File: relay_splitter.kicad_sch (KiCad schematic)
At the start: 7 parts, among them J10 Pads for coax, K6 RY-12W-K, Q6 MMBT3904

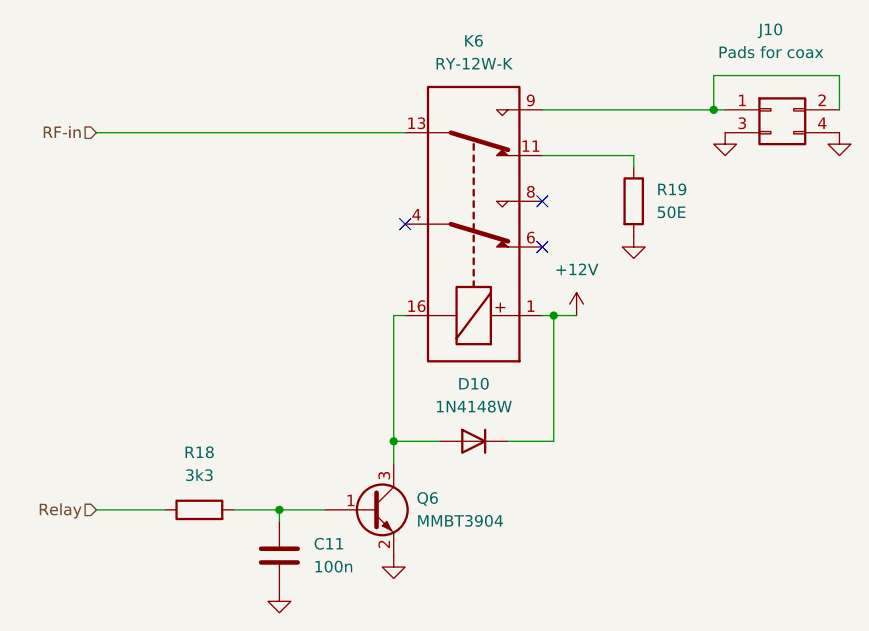
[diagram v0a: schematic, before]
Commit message: changed to 1 to 6
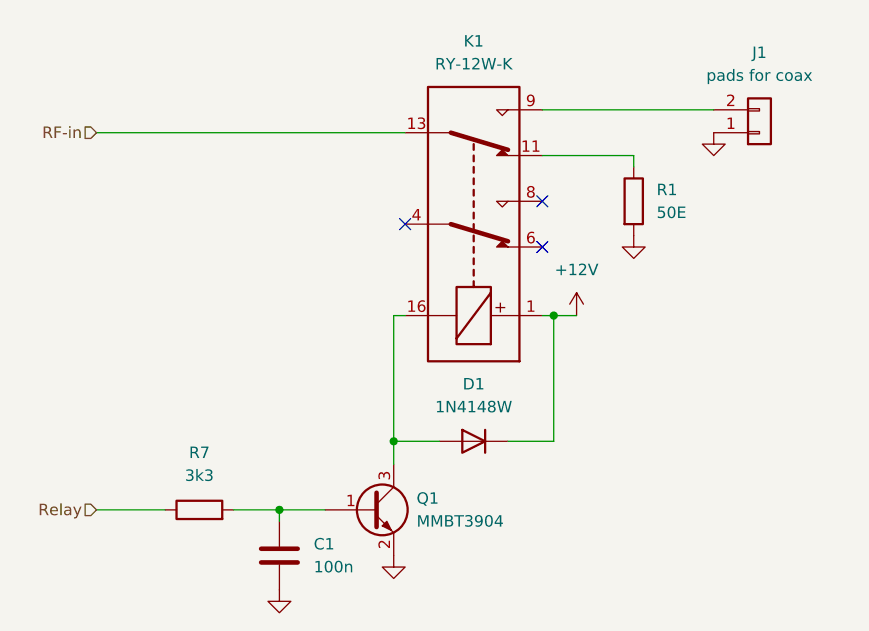
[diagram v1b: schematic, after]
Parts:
- removed J10: Pads for coax, Connector_PinHeader_2.54mm:PinHeader_2x02_P2.54mm_Vertical, symbol Components:Conn_02x02_Odd_Even
- added J1: pads for coax, Components:Coax_pad, symbol Components:Conn_01x02
- renumbered C11 to C1, D10 to D1, K6 to K1, Q6 to Q1, R19 to R1, R18 to R7
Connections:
- net GND: now also J1.1 (Pin_1)
- net at K1.9: now also J1.2 (Pin_2)
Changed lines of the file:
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@@
   (junction (at 127 107.95) (diameter 0) (color 0 0 0 0)
-  )
-  (junction (at 162.56 71.12) (diameter 0) (color 0 0 0 0)
   )
   (no_connect (at 128.27 83.82))
@@
     (stroke (width 0) (type default) (color 0 0 0 0))
   )
-  (wire (pts (xy 176.53 71.12) (xy 176.53 67.31))
-    (stroke (width 0) (type default) (color 0 0 0 0))
-  )
   (wire (pts (xy 127 110.49) (xy 127 107.95))
     (stroke (width 0) (type default) (color 0 0 0 0))
@@
     (stroke (width 0) (type default) (color 0 0 0 0))
   )
-  (wire (pts (xy 176.53 67.31) (xy 162.56 67.31))
-    (stroke (width 0) (type default) (color 0 0 0 0))
-  )
   (wire (pts (xy 153.67 76.2) (xy 153.67 77.47))
     (stroke (width 0) (type default) (color 0 0 0 0))
@@
     (stroke (width 0) (type default) (color 0 0 0 0))
   )
-  (wire (pts (xy 162.56 67.31) (xy 162.56 71.12))
-    (stroke (width 0) (type default) (color 0 0 0 0))
-  )
   (wire (pts (xy 93.98 73.66) (xy 128.27 73.66))
     (stroke (width 0) (type default) (color 0 0 0 0))
@@
   )
   (wire (pts (xy 143.51 71.12) (xy 162.56 71.12))
-    (stroke (width 0) (type default) (color 0 0 0 0))
-  )
-  (wire (pts (xy 162.56 71.12) (xy 163.83 71.12))
     (stroke (width 0) (type default) (color 0 0 0 0))
   )
@@
     (effects (font (size 1.27 1.27)) (justify right))
   )
-  (symbol (lib_id "power:GND") (at 176.53 73.66 0) (unit 1)
-    (in_bom yes) (on_board yes) (fields_autoplaced)
-    (property "Reference" "#PWR055" (id 0) (at 176.53 80.01 0)
-      (effects (font (size 1.27 1.27)) hide)
-    )
-    (property "Value" "GND" (id 1) (at 176.53 78.74 0)
-      (effects (font (size 1.27 1.27)) hide)
-    )
-    (property "Footprint" "" (id 2) (at 176.53 73.66 0)
-      (effects (font (size 1.27 1.27)) hide)
-    )
-    (property "Datasheet" "" (id 3) (at 176.53 73.66 0)
-      (effects (font (size 1.27 1.27)) hide)
-    )
-    (pin "1")
-  )
   (symbol (lib_id "power:+12V") (at 147.32 93.98 0) (unit 1)
     (in_bom yes) (on_board yes) (fields_autoplaced)
-    (property "Reference" "#PWR052" (id 0) (at 147.32 97.79 0)
+    (property "Reference" "#PWR045" (id 0) (at 147.32 97.79 0)
       (effects (font (size 1.27 1.27)) hide)
     )
@@
   (symbol (lib_id "Device:R") (at 105.41 115.57 90) (unit 1)
     (in_bom yes) (on_board yes) (fields_autoplaced)
-    (property "Reference" "R18" (id 0) (at 105.41 109.22 90))
+    (property "Reference" "R7" (id 0) (at 105.41 109.22 90))
     (property "Value" "3k3" (id 1) (at 105.41 111.76 90))
     (property "Footprint" "Resistor_SMD:R_0603_1608Metric_Pad0.98x0.95mm_HandSolder" (id 2) (at 105.41 117.348 90)
@@
   (symbol (lib_id "Transistor_BJT:MMBT3904") (at 124.46 115.57 0) (unit 1)
     (in_bom yes) (on_board yes) (fields_autoplaced)
-    (property "Reference" "Q6" (id 0) (at 129.54 114.2999 0)
+    (property "Reference" "Q1" (id 0) (at 129.54 114.2999 0)
       (effects (font (size 1.27 1.27)) (justify left))
     )
@@
     (pin "3")
   )
+  (symbol (lib_id "Components:Conn_01x02") (at 167.64 73.66 0) (mirror x) (unit 1)
+    (in_bom yes) (on_board yes) (fields_autoplaced)
+    (property "Reference" "J1" (id 0) (at 167.64 64.77 0))
+    (property "Value" "pads for coax" (id 1) (at 167.64 67.31 0))
+    (property "Footprint" "Components:Coax_pad" (id 2) (at 167.64 73.66 0)
+      (effects (font (size 1.27 1.27)) hide)
+    )
+    (property "Datasheet" "~" (id 3) (at 167.64 73.66 0)
+      (effects (font (size 1.27 1.27)) hide)
+    )
+    (pin "1")
+    (pin "2")
+  )
   (symbol (lib_id "Device:C") (at 114.3 120.65 0) (unit 1)
     (in_bom yes) (on_board yes) (fields_autoplaced)
-    (property "Reference" "C11" (id 0) (at 118.11 119.3799 0)
+    (property "Reference" "C1" (id 0) (at 118.11 119.3799 0)
       (effects (font (size 1.27 1.27)) (justify left))
     )
@@
     (pin "2")
   )
-  (symbol (lib_id "Components:Conn_02x02_Odd_Even") (at 168.91 71.12 0) (unit 1)
-    (in_bom yes) (on_board yes)
-    (property "Reference" "J10" (id 0) (at 168.91 62.23 0))
-    (property "Value" "Pads for coax" (id 1) (at 168.91 64.77 0))
-    (property "Footprint" "Connector_PinHeader_2.54mm:PinHeader_2x02_P2.54mm_Vertical" (id 2) (at 168.91 71.12 0)
-      (effects (font (size 1.27 1.27)) hide)
-    )
-    (property "Datasheet" "~" (id 3) (at 168.91 71.12 0)
-      (effects (font (size 1.27 1.27)) hide)
-    )
-    (pin "1")
-    (pin "2")
-    (pin "3")
-    (pin "4")
-  )
-  (symbol (lib_id "power:GND") (at 163.83 73.66 0) (unit 1)
-    (in_bom yes) (on_board yes) (fields_autoplaced)
-    (property "Reference" "#PWR054" (id 0) (at 163.83 80.01 0)
-      (effects (font (size 1.27 1.27)) hide)
-    )
-    (property "Value" "GND" (id 1) (at 163.83 78.74 0)
-      (effects (font (size 1.27 1.27)) hide)
-    )
-    (property "Footprint" "" (id 2) (at 163.83 73.66 0)
-      (effects (font (size 1.27 1.27)) hide)
-    )
-    (property "Datasheet" "" (id 3) (at 163.83 73.66 0)
-      (effects (font (size 1.27 1.27)) hide)
-    )
-    (pin "1")
-  )
   (symbol (lib_id "Components:RY-12W-K") (at 135.89 83.82 270) (mirror x) (unit 1)
     (in_bom yes) (on_board yes) (fields_autoplaced)
-    (property "Reference" "K6" (id 0) (at 135.89 63.5 90))
+    (property "Reference" "K1" (id 0) (at 135.89 63.5 90))
     (property "Value" "RY-12W-K" (id 1) (at 135.89 66.04 90))
     (property "Footprint" "Components:RELAY_RY-12W-K" (id 2) (at 137.16 69.85 0)
@@
   (symbol (lib_id "power:GND") (at 127 120.65 0) (unit 1)
     (in_bom yes) (on_board yes) (fields_autoplaced)
-    (property "Reference" "#PWR051" (id 0) (at 127 127 0)
+    (property "Reference" "#PWR044" (id 0) (at 127 127 0)
       (effects (font (size 1.27 1.27)) hide)
     )
@@
   (symbol (lib_id "Device:R") (at 153.67 81.28 0) (unit 1)
     (in_bom yes) (on_board yes) (fields_autoplaced)
-    (property "Reference" "R19" (id 0) (at 156.21 80.0099 0)
+    (property "Reference" "R1" (id 0) (at 156.21 80.0099 0)
       (effects (font (size 1.27 1.27)) (justify left))
     )
@@
   (symbol (lib_id "power:GND") (at 153.67 85.09 0) (unit 1)
     (in_bom yes) (on_board yes) (fields_autoplaced)
-    (property "Reference" "#PWR053" (id 0) (at 153.67 91.44 0)
+    (property "Reference" "#PWR046" (id 0) (at 153.67 91.44 0)
       (effects (font (size 1.27 1.27)) hide)
     )
@@
     (pin "1")
   )
+  (symbol (lib_id "power:GND") (at 162.56 73.66 0) (unit 1)
+    (in_bom yes) (on_board yes) (fields_autoplaced)
+    (property "Reference" "#PWR07" (id 0) (at 162.56 80.01 0)
+      (effects (font (size 1.27 1.27)) hide)
+    )
+    (property "Value" "GND" (id 1) (at 162.56 78.74 0)
+      (effects (font (size 1.27 1.27)) hide)
+    )
+    (property "Footprint" "" (id 2) (at 162.56 73.66 0)
+      (effects (font (size 1.27 1.27)) hide)
+    )
+    (property "Datasheet" "" (id 3) (at 162.56 73.66 0)
+      (effects (font (size 1.27 1.27)) hide)
+    )
+    (pin "1")
+  )
   (symbol (lib_id "power:GND") (at 114.3 124.46 0) (unit 1)
     (in_bom yes) (on_board yes) (fields_autoplaced)
-    (property "Reference" "#PWR050" (id 0) (at 114.3 130.81 0)
+    (property "Reference" "#PWR043" (id 0) (at 114.3 130.81 0)
       (effects (font (size 1.27 1.27)) hide)
     )
@@
   (symbol (lib_id "Diode:1N4148W") (at 135.89 107.95 0) (mirror y) (unit 1)
     (in_bom yes) (on_board yes) (fields_autoplaced)
-    (property "Reference" "D10" (id 0) (at 135.89 101.6 0))
+    (property "Reference" "D1" (id 0) (at 135.89 101.6 0))
     (property "Value" "1N4148W" (id 1) (at 135.89 104.14 0))
     (property "Footprint" "Diode_SMD:D_SOD-123" (id 2) (at 135.89 112.395 0)

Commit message: pcb routed and made gerbers
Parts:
- removed J1: pads for coax, Components:Coax_pad, symbol Components:Conn_01x02
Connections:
- net RF-out: now reaches K1.9
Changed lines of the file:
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@@
     (effects (font (size 1.27 1.27)) (justify right))
+  )
+  (hierarchical_label "RF-out" (shape output) (at 162.56 71.12 0)
+    (effects (font (size 1.27 1.27)) (justify left))
   )
   (hierarchical_label "Relay" (shape input) (at 93.98 115.57 180)
@@
     (pin "2")
     (pin "3")
-  )
-  (symbol (lib_id "Components:Conn_01x02") (at 167.64 73.66 0) (mirror x) (unit 1)
-    (in_bom yes) (on_board yes) (fields_autoplaced)
-    (property "Reference" "J1" (id 0) (at 167.64 64.77 0))
-    (property "Value" "pads for coax" (id 1) (at 167.64 67.31 0))
-    (property "Footprint" "Components:Coax_pad" (id 2) (at 167.64 73.66 0)
-      (effects (font (size 1.27 1.27)) hide)
-    )
-    (property "Datasheet" "~" (id 3) (at 167.64 73.66 0)
-      (effects (font (size 1.27 1.27)) hide)
-    )
-    (pin "1")
-    (pin "2")
   )
   (symbol (lib_id "Device:C") (at 114.3 120.65 0) (unit 1)
@@
       (effects (font (size 1.27 1.27)) hide)
     )
-    (pin "1")
-  )
-  (symbol (lib_id "power:GND") (at 162.56 73.66 0) (unit 1)
-    (in_bom yes) (on_board yes) (fields_autoplaced)
-    (property "Reference" "#PWR07" (id 0) (at 162.56 80.01 0)
-      (effects (font (size 1.27 1.27)) hide)
-    )
-    (property "Value" "GND" (id 1) (at 162.56 78.74 0)
-      (effects (font (size 1.27 1.27)) hide)
-    )
-    (property "Footprint" "" (id 2) (at 162.56 73.66 0)
-      (effects (font (size 1.27 1.27)) hide)
-    )
-    (property "Datasheet" "" (id 3) (at 162.56 73.66 0)
-      (effects (font (size 1.27 1.27)) hide)
-    )

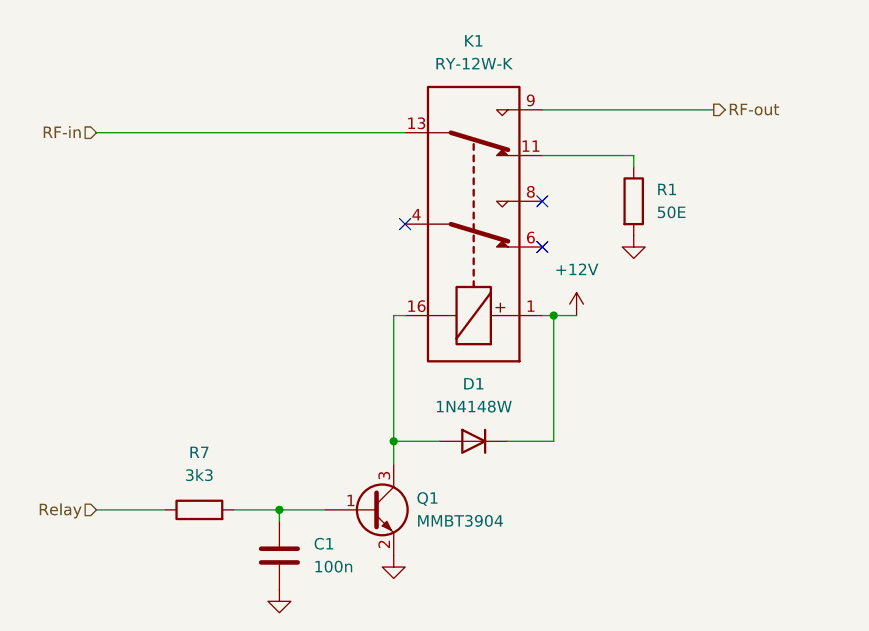
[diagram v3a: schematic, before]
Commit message: used both contacts on relays
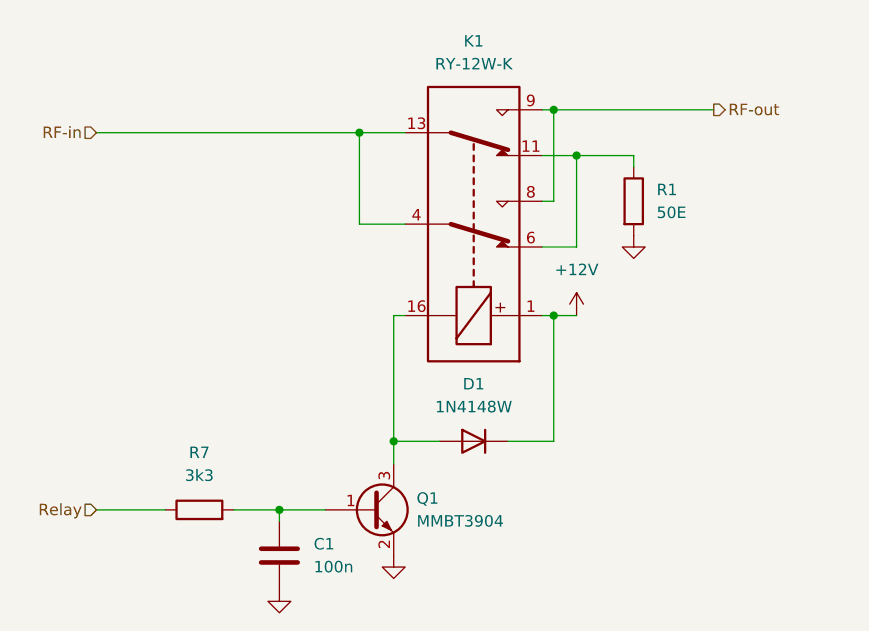
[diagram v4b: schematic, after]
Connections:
- net RF-in: now also K1.4
- net RF-out: now also K1.8
- net at K1.11, R1.1: now also K1.6
- no-connect marks 3 -> 0
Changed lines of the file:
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@@
   (junction (at 144.78 93.98) (diameter 0) (color 0 0 0 0)
+  )
+  (junction (at 123.19 73.66) (diameter 0) (color 0 0 0 0)
+  )
+  (junction (at 147.32 76.2) (diameter 0) (color 0 0 0 0)
+  )
+  (junction (at 144.78 71.12) (diameter 0) (color 0 0 0 0)
   )
   (junction (at 127 107.95) (diameter 0) (color 0 0 0 0)
   )
-  (no_connect (at 128.27 83.82))
-  (no_connect (at 143.51 81.28))
-  (no_connect (at 143.51 86.36))
-  (wire (pts (xy 143.51 76.2) (xy 153.67 76.2))
+  (wire (pts (xy 144.78 81.28) (xy 144.78 71.12))
+    (stroke (width 0) (type default) (color 0 0 0 0))
+  )
+  (wire (pts (xy 123.19 73.66) (xy 128.27 73.66))
+    (stroke (width 0) (type default) (color 0 0 0 0))
+  )
+  (wire (pts (xy 147.32 76.2) (xy 153.67 76.2))
+    (stroke (width 0) (type default) (color 0 0 0 0))
+  )
+  (wire (pts (xy 143.51 76.2) (xy 147.32 76.2))
     (stroke (width 0) (type default) (color 0 0 0 0))
   )
   (wire (pts (xy 139.7 107.95) (xy 144.78 107.95))
+    (stroke (width 0) (type default) (color 0 0 0 0))
+  )
+  (wire (pts (xy 143.51 86.36) (xy 147.32 86.36))
+    (stroke (width 0) (type default) (color 0 0 0 0))
+  )
+  (wire (pts (xy 143.51 81.28) (xy 144.78 81.28))
     (stroke (width 0) (type default) (color 0 0 0 0))
   )
@@
     (stroke (width 0) (type default) (color 0 0 0 0))
   )
+  (wire (pts (xy 128.27 83.82) (xy 123.19 83.82))
+    (stroke (width 0) (type default) (color 0 0 0 0))
+  )
   (wire (pts (xy 127 110.49) (xy 127 107.95))
     (stroke (width 0) (type default) (color 0 0 0 0))
@@
     (stroke (width 0) (type default) (color 0 0 0 0))
   )
+  (wire (pts (xy 123.19 73.66) (xy 123.19 83.82))
+    (stroke (width 0) (type default) (color 0 0 0 0))
+  )
   (wire (pts (xy 109.22 115.57) (xy 114.3 115.57))
+    (stroke (width 0) (type default) (color 0 0 0 0))
+  )
+  (wire (pts (xy 147.32 86.36) (xy 147.32 76.2))
     (stroke (width 0) (type default) (color 0 0 0 0))
   )
@@
     (stroke (width 0) (type default) (color 0 0 0 0))
   )
-  (wire (pts (xy 93.98 73.66) (xy 128.27 73.66))
+  (wire (pts (xy 93.98 73.66) (xy 123.19 73.66))
     (stroke (width 0) (type default) (color 0 0 0 0))
   )
@@
     (stroke (width 0) (type default) (color 0 0 0 0))
   )
-  (wire (pts (xy 143.51 71.12) (xy 162.56 71.12))
+  (wire (pts (xy 143.51 71.12) (xy 144.78 71.12))
     (stroke (width 0) (type default) (color 0 0 0 0))
   )
+  (wire (pts (xy 144.78 71.12) (xy 162.56 71.12))
+    (stroke (width 0) (type default) (color 0 0 0 0))
+  )
